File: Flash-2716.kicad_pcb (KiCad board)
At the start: 2 copper layers, 19.1 x 50.8 mm, 12 parts, among them J1 Conn_01x12, J2 Conn_01x12, U1 SST39SF010

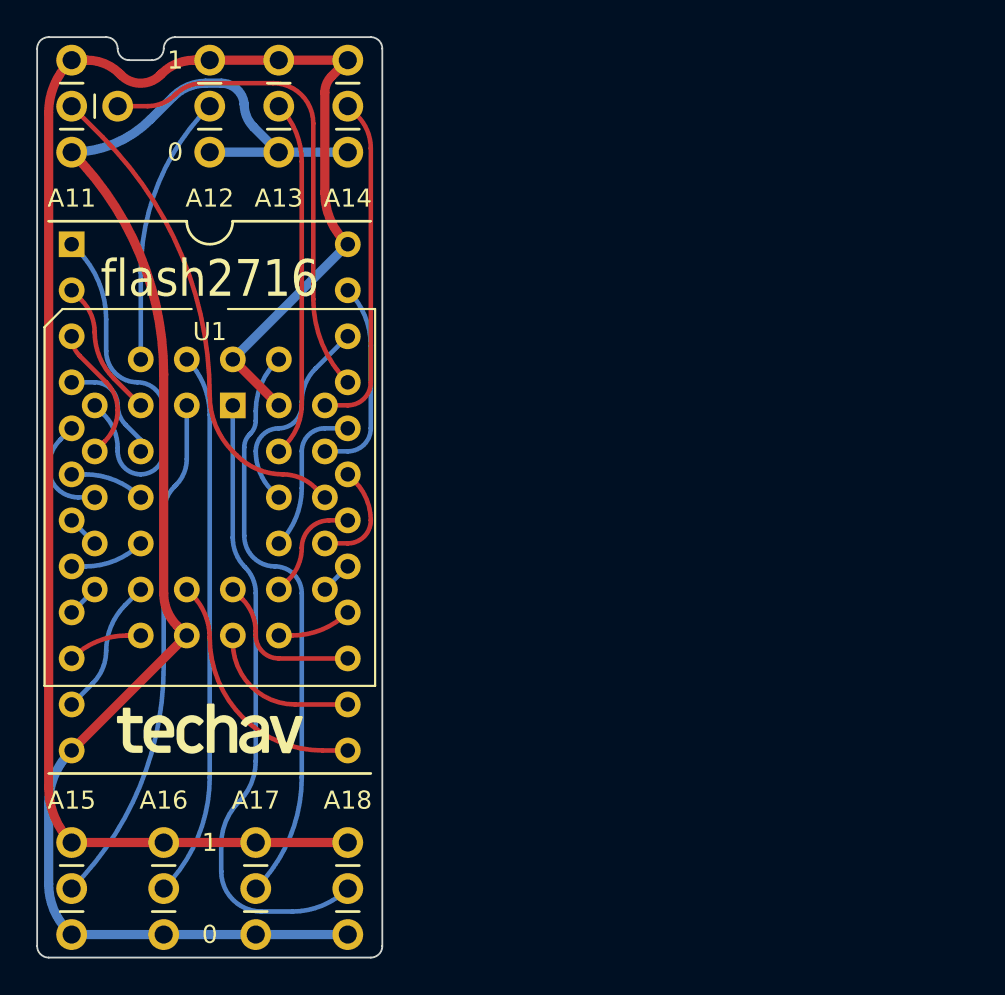
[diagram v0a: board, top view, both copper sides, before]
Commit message: Add 2716 socket & storage
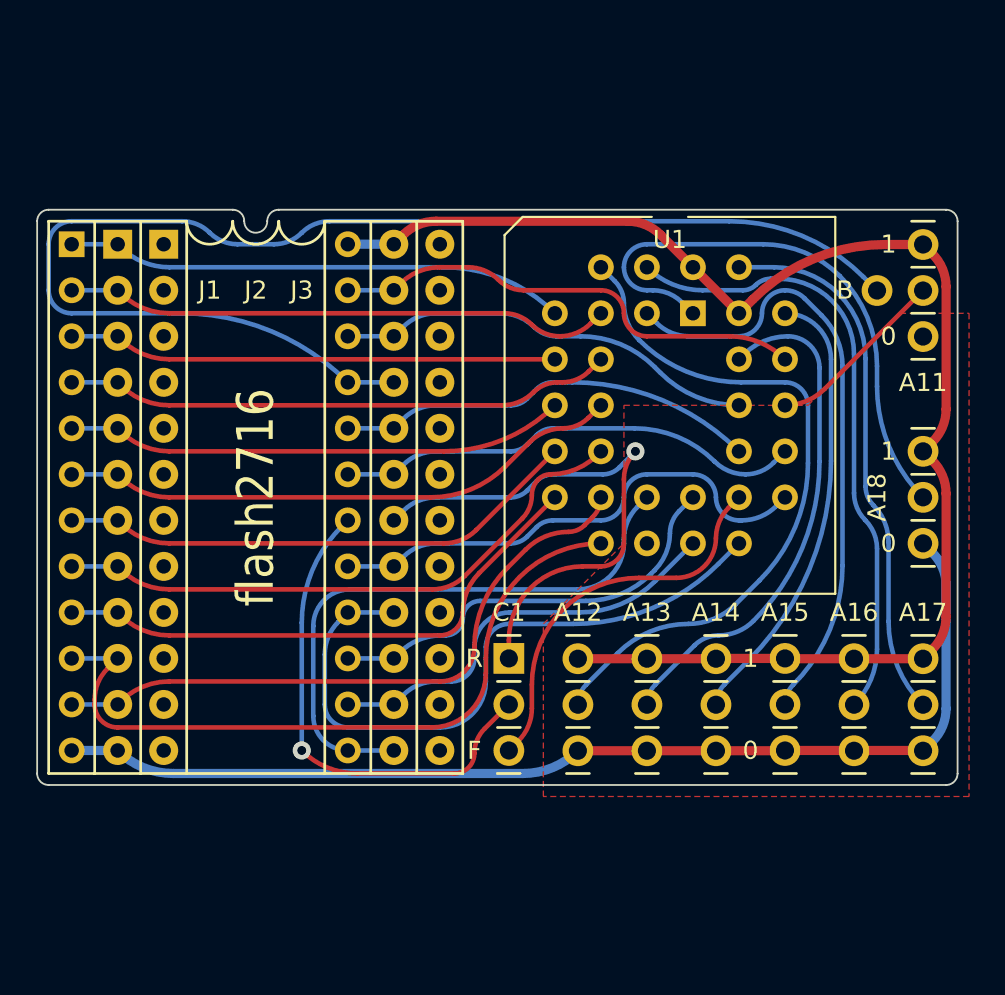
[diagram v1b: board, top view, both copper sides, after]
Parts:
- added C1: Jumper_3_Open, Connector_PinHeader_2.54mm:PinHeader_1x03_P2.54mm_Vertical, F.Cu at (125.7, 99.1)
- added J2: 2716, Package_DIP:DIP-24_W15.24mm_Socket, F.Cu at (104.1, 76.2)
- added J3: 2716, Package_DIP:DIP-24_W15.24mm_Socket, F.Cu at (106.7, 76.2)
- moved A11 48.1 mm to (148.6, 76.2)
- moved JP1 43.1 mm to (146.1, 78.8)
- moved A15 40.7 mm to (141.0, 99.1)
- moved A16 39.4 mm to (144.8, 99.1)
- moved A12 38.8 mm to (129.5, 99.1)
- moved A13 38.8 mm to (133.3, 99.1)
- moved A14 38.8 mm to (137.2, 99.1)
- moved A18 38.4 mm to (148.6, 87.6)
- moved A17 38.2 mm to (148.6, 99.1)
- moved U1 25.9 mm to (135.9, 80.0)
- renumbered J2 to J4
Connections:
- J4 pad 7: /~{CE} -> /~{BUS-CE}
- U1 pad 22: /~{CE} -> /~{CE-39}
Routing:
- net /BUS-A11: track 27.1 -> 71.3 mm
- net /D1: track 4.13 -> 39.9 mm
- net /D6: track 4.12 -> 36.8 mm
- net /~{CE-27}: track 0.00 -> 30.0 mm, vias 0 -> 1
- net /D0: track 1.80 -> 30.9 mm
- net /A0: track 4.13 -> 33.0 mm
- net /D2: track 7.63 -> 35.3 mm
- net /~{BUS-CE}: track 0.00 -> 27.2 mm, vias 0 -> 1
- net /A1: track 1.80 -> 29.0 mm
- net /A2: track 4.13 -> 31.2 mm
- net /D7: track 1.80 -> 28.0 mm
- net GND: track 85.6 -> 59.9 mm
- net /A4: track 6.21 -> 30.3 mm
- net /A12: track 14.9 -> 38.3 mm
- net /A6: track 7.64 -> 30.3 mm
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- added copper zone on F.Cu, net GND
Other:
- board size 19.1 x 50.8 mm -> 50.8 x 31.8 mm
- board text added: "B"
- board text added: "C1-R: EPROM C1-F: Flash"
- board text added: "F"
- board text added: "J1"
- board text added: "J1: To Board J2: Pass-through J3: No connect (storage)"
- board text added: "R"

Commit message: Cleanup & plot gerbers
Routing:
- net /A12: track 38.3 -> 42.2 mm
- net /~{CE-39}: track 21.1 -> 20.5 mm
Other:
- board text added: "This is the back"
